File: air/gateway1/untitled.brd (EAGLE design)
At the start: 106 x 74 mm, 41 parts, among them J1 10118193-0001LF, K1 351, Q2 MMBT3904, Q3 MMBT3904, Q4 S9013, U1 CH340G, U2 ESP32-WROOM-32D, U3 AMS1117, U4 PC817X2NIP0F, X2 MSTBA3, X3 MSTBA3

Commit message: fix PCB
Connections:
- net M1: now also U2.10
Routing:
- net M1: track 0.00 -> 279.8 mm, vias 0 -> 1
- net CONFIG_LORA: track 34.3 -> 36.9 mm
- net VUSB: track 226.7 -> 228.1 mm
- net GND: track 346.6 -> 345.4 mm
- net RXLORA_MICRO: track 51.6 -> 50.8 mm

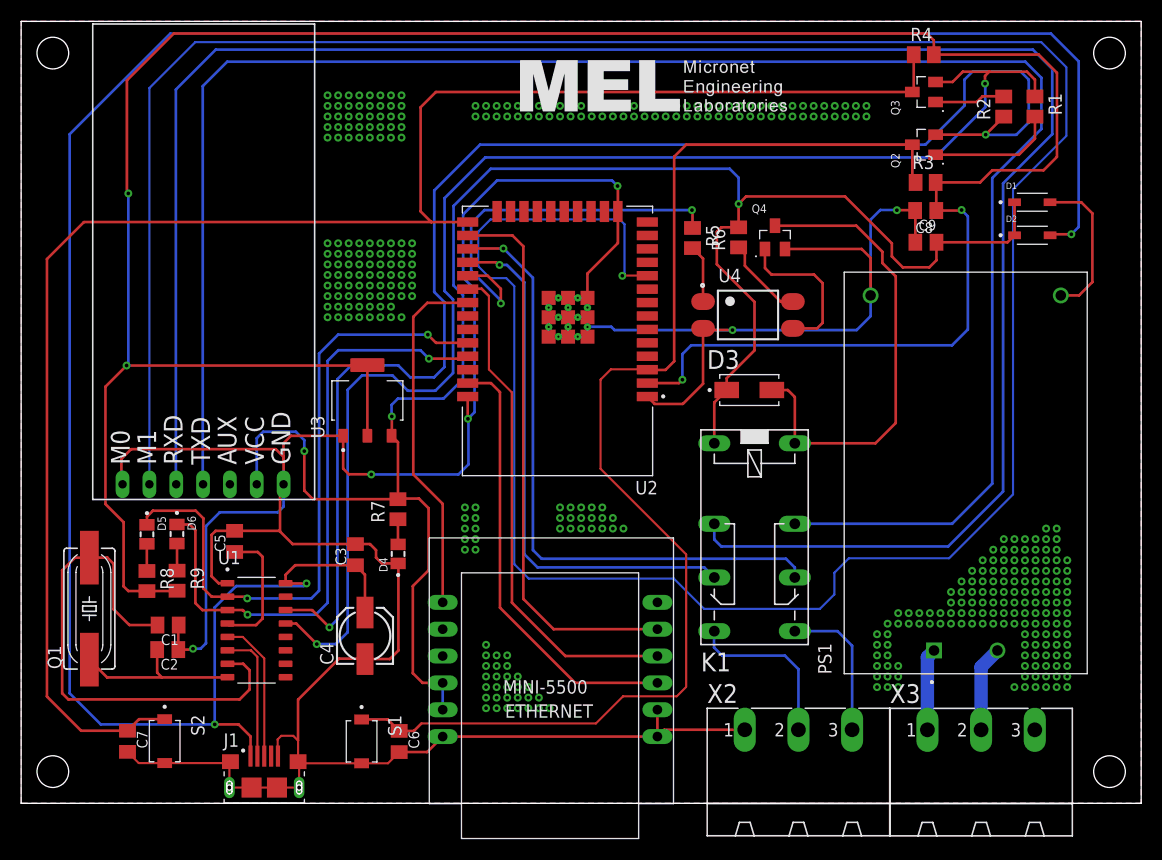
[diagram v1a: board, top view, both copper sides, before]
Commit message: fix PCB gateway box lama
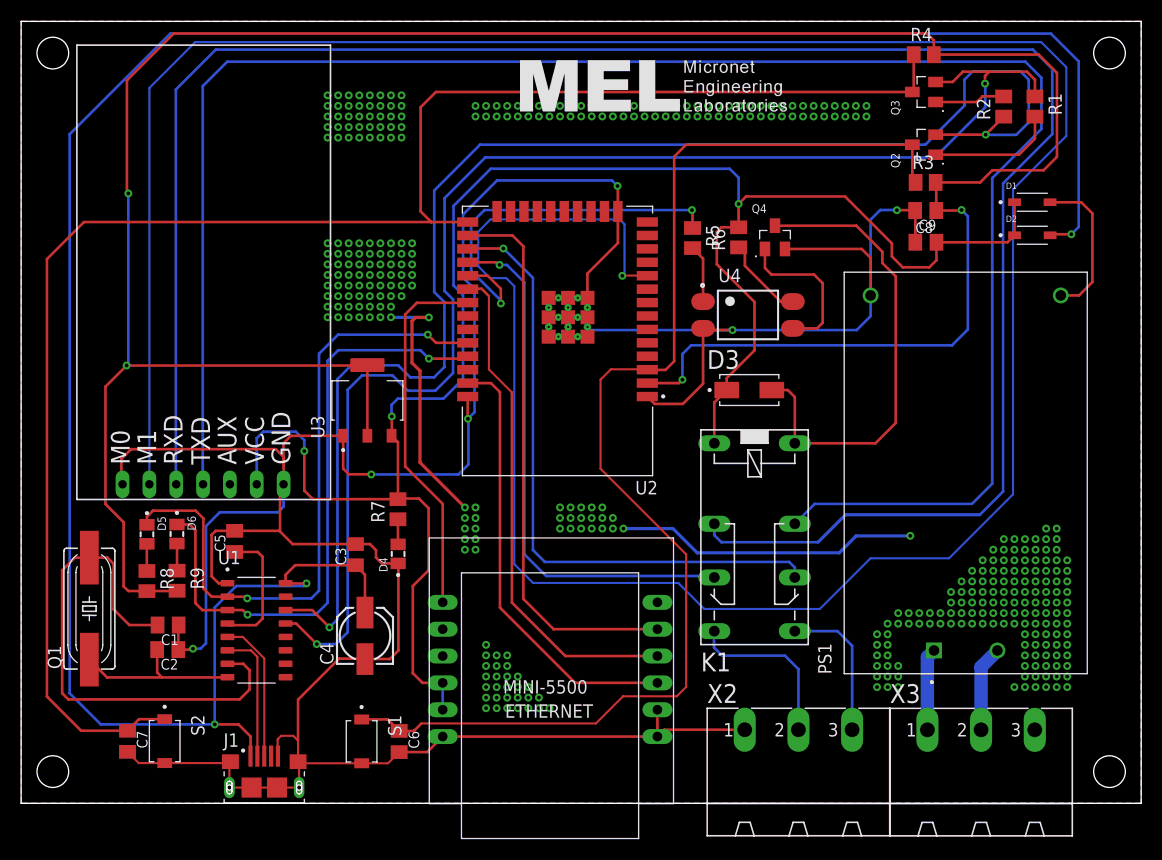
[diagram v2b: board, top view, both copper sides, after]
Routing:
- net N: track 0.00 -> 53.8 mm
- net MISO_VSPI: track 33.9 -> 35.1 mm
- net M1: track 279.8 -> 278.6 mm
- net RX_LORA: track 195.8 -> 195.2 mm
